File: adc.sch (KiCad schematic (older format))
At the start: 4 parts, among them U2 ADS114S08BIPBS

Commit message: added layout and online BOM viewer
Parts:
- C2, C3, C4: footprint (none) -> Capacitor_SMD:C_0805_2012Metric_Pad1.15x1.40mm_HandSolder
- U2: footprint PBS0032A_N -> footprints:ADS114S08BIPBS
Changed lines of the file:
@@
 $Descr A4 11693 8268
 encoding utf-8
-Sheet 2 3
+Sheet 3 3
 Title ""
 Date ""
@@
 AR Path="/5F3793F6/5F379707" Ref="U2"  Part="1"
 AR Path="/5F3BC575/5F379707" Ref="U3"  Part="1"
-F 0 "U2" H 4550 5488 60  0000 C CNN
+F 0 "U3" H 4550 5488 60  0000 C CNN
 F 1 "ADS114S08BIPBS" H 4550 5382 60  0000 C CNN
-F 2 "PBS0032A_N" H 4550 3640 60  0001 C CNN
+F 2 "footprints:ADS114S08BIPBS" H 4550 3640 60  0001 C CNN
 F 3 "" H 4550 3700 60  0000 C CNN
 	1    4550 3700
@@
 AR Path="/5F3793F6/5F37A378" Ref="C3"  Part="1"
 AR Path="/5F3BC575/5F37A378" Ref="C6"  Part="1"
-F 0 "C3" H 5992 2596 50  0000 L CNN
+F 0 "C6" H 5992 2596 50  0000 L CNN
 F 1 "1uF" H 5992 2505 50  0000 L CNN
-F 2 "" H 5900 2550 50  0001 C CNN
+F 2 "Capacitor_SMD:C_0805_2012Metric_Pad1.15x1.40mm_HandSolder" H 5900 2550 50  0001 C CNN
 F 3 "~" H 5900 2550 50  0001 C CNN
 	1    5900 2550
@@
 AR Path="/5F3793F6/5F37B0A0" Ref="C2"  Part="1"
 AR Path="/5F3BC575/5F37B0A0" Ref="C5"  Part="1"
-F 0 "C2" H 3242 4746 50  0000 L CNN
+F 0 "C5" H 3242 4746 50  0000 L CNN
 F 1 "330nF" H 3242 4655 50  0000 L CNN
-F 2 "" H 3150 4700 50  0001 C CNN
+F 2 "Capacitor_SMD:C_0805_2012Metric_Pad1.15x1.40mm_HandSolder" H 3150 4700 50  0001 C CNN
 F 3 "~" H 3150 4700 50  0001 C CNN
 	1    3150 4700
@@
 AR Path="/5F3793F6/5F389336" Ref="#PWR0105"  Part="1"
 AR Path="/5F3BC575/5F389336" Ref="#PWR0114"  Part="1"
-F 0 "#PWR0105" H 3150 4450 50  0001 C CNN
+F 0 "#PWR0114" H 3150 4450 50  0001 C CNN
 F 1 "+5V" H 3165 4773 50  0000 C CNN
 F 2 "" H 3150 4600 50  0001 C CNN
@@
 AR Path="/5F3793F6/5F38A513" Ref="#PWR0106"  Part="1"
 AR Path="/5F3BC575/5F38A513" Ref="#PWR0115"  Part="1"
-F 0 "#PWR0106" H 6000 4450 50  0001 C CNN
+F 0 "#PWR0115" H 6000 4450 50  0001 C CNN
 F 1 "+3.3V" H 6015 4773 50  0000 C CNN
 F 2 "" H 6000 4600 50  0001 C CNN
@@
 AR Path="/5F3793F6/5F38BAFC" Ref="C4"  Part="1"
 AR Path="/5F3BC575/5F38BAFC" Ref="C7"  Part="1"
-F 0 "C4" H 6092 4746 50  0000 L CNN
+F 0 "C7" H 6092 4746 50  0000 L CNN
 F 1 "0.1uF" H 6092 4655 50  0000 L CNN
-F 2 "" H 6000 4700 50  0001 C CNN
+F 2 "Capacitor_SMD:C_0805_2012Metric_Pad1.15x1.40mm_HandSolder" H 6000 4700 50  0001 C CNN
 F 3 "~" H 6000 4700 50  0001 C CNN
 	1    6000 4700
@@
 AR Path="/5F3793F6/5F38C9D2" Ref="#PWR0107"  Part="1"
 AR Path="/5F3BC575/5F38C9D2" Ref="#PWR0116"  Part="1"
-F 0 "#PWR0107" H 3150 4650 50  0001 C CNN
+F 0 "#PWR0116" H 3150 4650 50  0001 C CNN
 F 1 "GND" H 3155 4727 50  0000 C CNN
 F 2 "" H 3150 4900 50  0001 C CNN
@@
 AR Path="/5F3793F6/5F38E020" Ref="#PWR0108"  Part="1"
 AR Path="/5F3BC575/5F38E020" Ref="#PWR0117"  Part="1"
-F 0 "#PWR0108" H 6000 4850 50  0001 C CNN
+F 0 "#PWR0117" H 6000 4850 50  0001 C CNN
 F 1 "GND" H 6005 4927 50  0000 C CNN
 F 2 "" H 6000 5100 50  0001 C CNN
@@
 AR Path="/5F3793F6/5F38F179" Ref="#PWR0109"  Part="1"
 AR Path="/5F3BC575/5F38F179" Ref="#PWR0118"  Part="1"
-F 0 "#PWR0109" H 5900 2450 50  0001 C CNN
+F 0 "#PWR0118" H 5900 2450 50  0001 C CNN
 F 1 "GND" H 5905 2527 50  0000 C CNN
 F 2 "" H 5900 2700 50  0001 C CNN
@@
 AR Path="/5F3793F6/5F38F87E" Ref="#PWR0110"  Part="1"
 AR Path="/5F3BC575/5F38F87E" Ref="#PWR0119"  Part="1"
-F 0 "#PWR0110" H 5900 2950 50  0001 C CNN
+F 0 "#PWR0119" H 5900 2950 50  0001 C CNN
 F 1 "GND" H 5905 3027 50  0000 C CNN
 F 2 "" H 5900 3200 50  0001 C CNN
@@
 AR Path="/5F3793F6/5F39184B" Ref="#PWR0111"  Part="1"
 AR Path="/5F3BC575/5F39184B" Ref="#PWR0120"  Part="1"
-F 0 "#PWR0111" H 3100 2650 50  0001 C CNN
+F 0 "#PWR0120" H 3100 2650 50  0001 C CNN
 F 1 "GND" H 3105 2727 50  0000 C CNN
 F 2 "" H 3100 2900 50  0001 C CNN
@@
 AR Path="/5F3793F6/5F39364B" Ref="#PWR0112"  Part="1"
 AR Path="/5F3BC575/5F39364B" Ref="#PWR0121"  Part="1"
-F 0 "#PWR0112" H 6550 4350 50  0001 C CNN
+F 0 "#PWR0121" H 6550 4350 50  0001 C CNN
 F 1 "GND" H 6555 4427 50  0000 C CNN
 F 2 "" H 6550 4600 50  0001 C CNN
@@
 AR Path="/5F3793F6/5F394587" Ref="#PWR0113"  Part="1"
 AR Path="/5F3BC575/5F394587" Ref="#PWR0122"  Part="1"
-F 0 "#PWR0113" H 6450 2550 50  0001 C CNN
+F 0 "#PWR0122" H 6450 2550 50  0001 C CNN
 F 1 "+3.3V" H 6465 2873 50  0000 C CNN
 F 2 "" H 6450 2700 50  0001 C CNN

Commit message: ads1261
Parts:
- removed C2: 330nF, Capacitor_SMD:C_0805_2012Metric_Pad1.15x1.40mm_HandSolder, symbol Device:C_Small
- removed C3: 1uF, Capacitor_SMD:C_0805_2012Metric_Pad1.15x1.40mm_HandSolder, symbol Device:C_Small
- removed C4: 0.1uF, Capacitor_SMD:C_0805_2012Metric_Pad1.15x1.40mm_HandSolder, symbol Device:C_Small
- removed U2: ADS114S08BIPBS, footprints:ADS114S08BIPBS, symbol ads114s08b:ADS114S08BIPBS
- added C202, C204, C205: 1uF, Capacitor_SMD:C_0603_1608Metric, symbol Device:C
- added C301: 4.7nF C0G, Capacitor_SMD:C_0603_1608Metric, symbol Device:C
- added C303, C306: 10uF, Capacitor_SMD:C_0603_1608Metric, symbol Device:C
- added U301: ADS1261BIRHBR, footprints:ADS1261BIRHBR, symbol ads1261:ADS1261BIRHBR
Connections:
- net labels added: AIN-, AIN0, AIN1, AIN2, AIN3, AIN4, AIN5, AIN6, AIN7, AIN8, AIN9, BYPASS, CAP+, CAP-, GNDREF, REF2.5V
- net labels removed: +2.5V_OUT, 0, 1, 10, 11, 2, 3, 4, 5, 6, 7, 8, 9, A0, A1, A10, A11, A2, A3, A4, A5, A6, A7, A8, A9
- wire segments 31 -> 30
- no-connect marks 4 -> 1
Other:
- note removed: "Calculating your voltage ranges:\nhttps://www.ti.com/tool/ADS124S08-EXCEL-CALC-TOOL"
- note removed: "The ADC is configured to operate in SPI command only mode\n"
- note removed: "This 2.5V out provides a good negative input\nfor sensors that rely on the PGA"
- note removed: "We will select the internal\n2.5V reference"
- note removed: "You call it "parasitic capacitance"\nTI calls it "integrated EMI filter"\n\nEither way I decided not to put RC filters on the ADC inputs since Freq. \nResponse is capped at 40 MHz\n (radio is 400ish Mhz). \nIf there is noise we can add external low \npass filters\n or use differential inputs to filter out common mode noise"

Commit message: boi did i cut up that ground plane
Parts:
- added R201: 4.7K, Resistor_SMD:R_0805_2012Metric_Pad1.15x1.40mm_HandSolder, symbol Device:R_US
- C202, C204, C205, C301, C303, C306: footprint Capacitor_SMD:C_0603_1608Metric -> Capacitor_SMD:C_0805_2012Metric_Pad1.15x1.40mm_HandSolder
- U301: footprint footprints:ADS1261BIRHBR -> Package_DFN_QFN:Texas_S-PVQFN-N32_EP3.45x3.45mm
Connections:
- net +3V3: now also R201.1
- net ~CS: now also R201.2
- net AIN- renamed AINCOM
- no-connect marks 1 -> 5

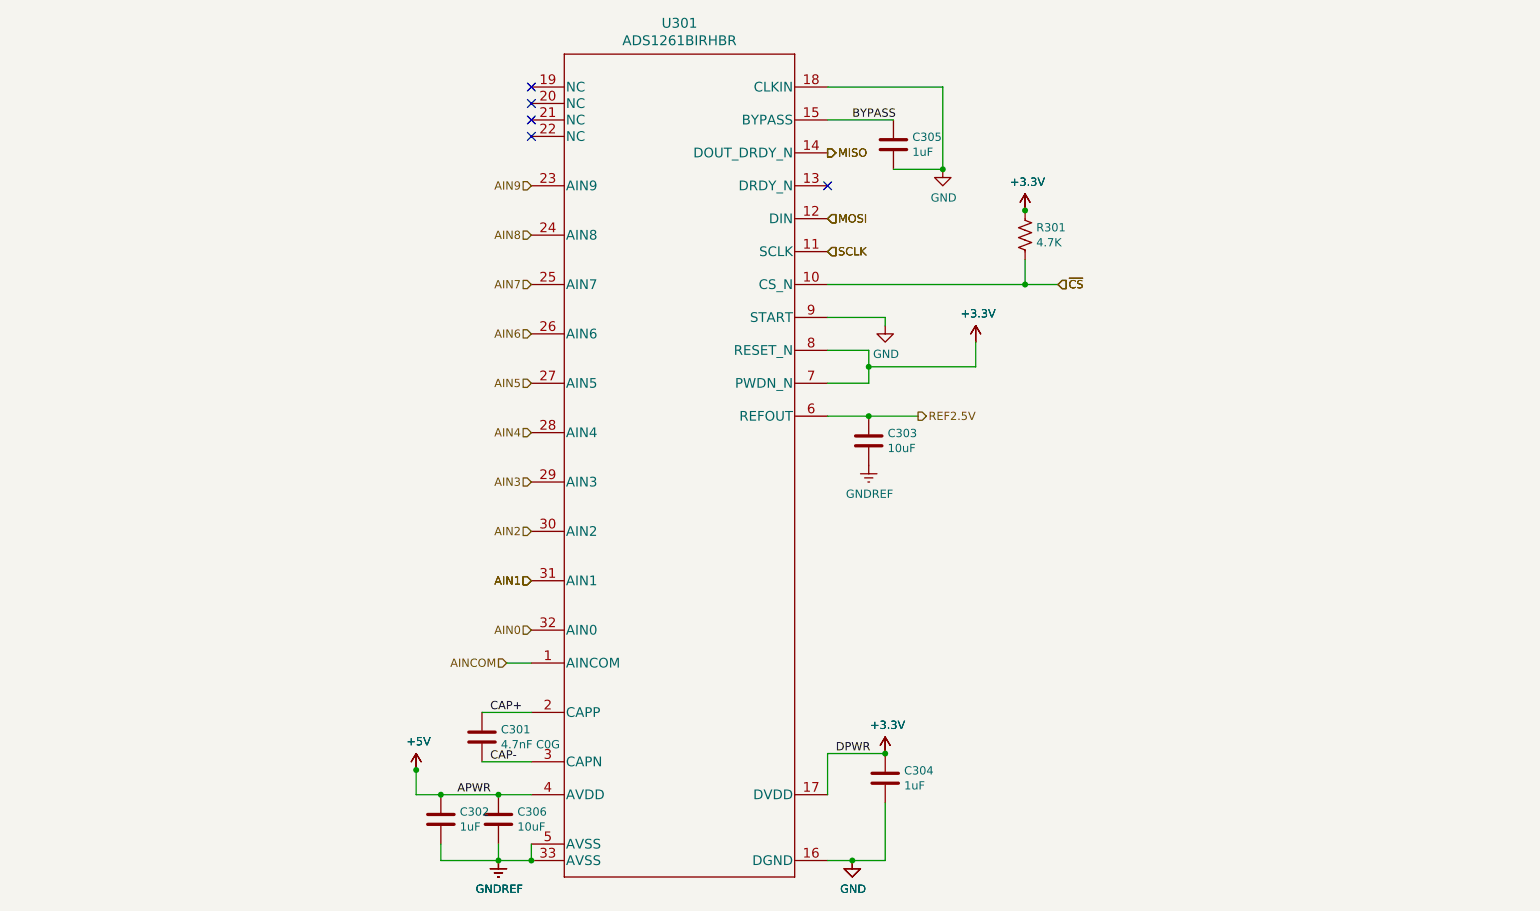
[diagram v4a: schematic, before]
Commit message: add silkscreen labels
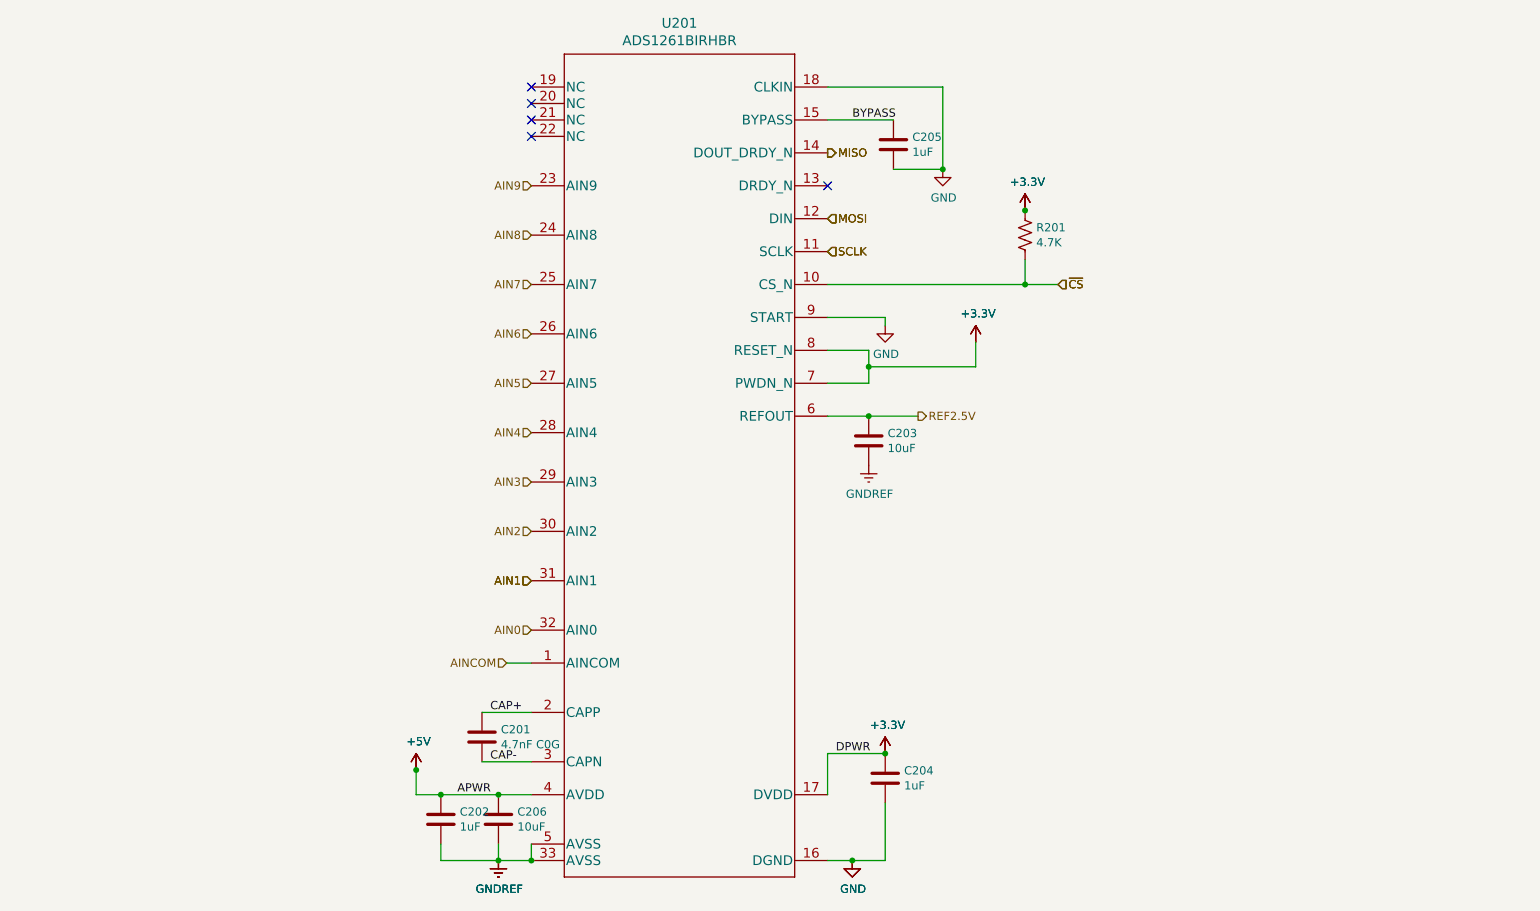
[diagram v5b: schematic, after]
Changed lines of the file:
@@
 $Descr A4 11693 8268
 encoding utf-8
-Sheet 3 4
+Sheet 2 4
 Title ""
 Date ""
@@
 AR Path="/5F4A8EC5/5F4D602B" Ref="#PWR0107"  Part="1"
 AR Path="/5F4D3EB7/5F4D602B" Ref="#PWR0123"  Part="1"
-F 0 "#PWR0123" H 3200 5600 50  0001 C CNN
+F 0 "#PWR0107" H 3200 5600 50  0001 C CNN
 F 1 "+5V" H 3215 5923 50  0000 C CNN
 F 2 "" H 3200 5750 50  0001 C CNN
@@
 AR Path="/5F4A8EC5/5F4ADFB1" Ref="#PWR0108"  Part="1"
 AR Path="/5F4D3EB7/5F4ADFB1" Ref="#PWR0124"  Part="1"
-F 0 "#PWR0124" H 3700 6050 50  0001 C CNN
+F 0 "#PWR0108" H 3700 6050 50  0001 C CNN
 F 1 "GNDREF" H 3705 6127 50  0000 C CNN
 F 2 "" H 3700 6300 50  0001 C CNN
@@
 AR Path="/5F4A8EC5/5F4AF0E5" Ref="#PWR0109"  Part="1"
 AR Path="/5F4D3EB7/5F4AF0E5" Ref="#PWR0125"  Part="1"
-F 0 "#PWR0125" H 5850 6050 50  0001 C CNN
+F 0 "#PWR0109" H 5850 6050 50  0001 C CNN
 F 1 "GND" H 5855 6127 50  0000 C CNN
 F 2 "" H 5850 6300 50  0001 C CNN
@@
 AR Path="/5F4A8EC5/5F4B0081" Ref="#PWR0110"  Part="1"
 AR Path="/5F4D3EB7/5F4B0081" Ref="#PWR0126"  Part="1"
-F 0 "#PWR0126" H 6050 5500 50  0001 C CNN
+F 0 "#PWR0110" H 6050 5500 50  0001 C CNN
 F 1 "+3.3V" H 6065 5823 50  0000 C CNN
 F 2 "" H 6050 5650 50  0001 C CNN
@@
 AR Path="/5F4A8EC5/5F4D6031" Ref="#PWR0113"  Part="1"
 AR Path="/5F4D3EB7/5F4D6031" Ref="#PWR0129"  Part="1"
-F 0 "#PWR0129" H 6600 3000 50  0001 C CNN
+F 0 "#PWR0113" H 6600 3000 50  0001 C CNN
 F 1 "+3.3V" H 6615 3323 50  0000 C CNN
 F 2 "" H 6600 3150 50  0001 C CNN
@@
 AR Path="/5F4A8EC5/5F4B6004" Ref="C205"  Part="1"
 AR Path="/5F4D3EB7/5F4B6004" Ref="C305"  Part="1"
-F 0 "C305" H 6215 1996 50  0000 L CNN
+F 0 "C205" H 6215 1996 50  0000 L CNN
 F 1 "1uF" H 6215 1905 50  0000 L CNN
 F 2 "Capacitor_SMD:C_0805_2012Metric_Pad1.15x1.40mm_HandSolder" H 6138 1800 50  0001 C CNN
@@
 AR Path="/5F4D3EB7/5F4A90E1" Ref="U301"  Part="1"
 AR Path="/5F4A8EC5/5F4A90E1" Ref="U201"  Part="1"
-F 0 "U301" H 4800 6588 60  0000 C CNN
+F 0 "U201" H 4800 6588 60  0000 C CNN
 F 1 "ADS1261BIRHBR" H 4800 6482 60  0000 C CNN
 F 2 "Package_DFN_QFN:Texas_S-PVQFN-N32_EP3.45x3.45mm" H 4800 3840 60  0001 C CNN
@@
 AR Path="/5F4D3EB7/5F4AAB9D" Ref="C301"  Part="1"
 AR Path="/5F4A8EC5/5F4AAB9D" Ref="C201"  Part="1"
-F 0 "C301" H 3715 5596 50  0000 L CNN
+F 0 "C201" H 3715 5596 50  0000 L CNN
 F 1 "4.7nF C0G" H 3715 5505 50  0000 L CNN
 F 2 "Capacitor_SMD:C_0805_2012Metric_Pad1.15x1.40mm_HandSolder" H 3638 5400 50  0001 C CNN
@@
 AR Path="/5F4D3EB7/5F4ABE0F" Ref="#PWR0131"  Part="1"
 AR Path="/5F4A8EC5/5F4ABE0F" Ref="#PWR0115"  Part="1"
-F 0 "#PWR0131" H 3200 5600 50  0001 C CNN
+F 0 "#PWR0115" H 3200 5600 50  0001 C CNN
 F 1 "+5V" H 3215 5923 50  0000 C CNN
 F 2 "" H 3200 5750 50  0001 C CNN
@@
 AR Path="/5F4D3EB7/5F4D602C" Ref="#PWR0132"  Part="1"
 AR Path="/5F4A8EC5/5F4D602C" Ref="#PWR0116"  Part="1"
-F 0 "#PWR0132" H 3700 6050 50  0001 C CNN
+F 0 "#PWR0116" H 3700 6050 50  0001 C CNN
 F 1 "GNDREF" H 3705 6127 50  0000 C CNN
 F 2 "" H 3700 6300 50  0001 C CNN
@@
 AR Path="/5F4D3EB7/5F4D602D" Ref="#PWR0133"  Part="1"
 AR Path="/5F4A8EC5/5F4D602D" Ref="#PWR0117"  Part="1"
-F 0 "#PWR0133" H 5850 6050 50  0001 C CNN
+F 0 "#PWR0117" H 5850 6050 50  0001 C CNN
 F 1 "GND" H 5855 6127 50  0000 C CNN
 F 2 "" H 5850 6300 50  0001 C CNN
@@
 AR Path="/5F4D3EB7/5F4D602E" Ref="#PWR0134"  Part="1"
 AR Path="/5F4A8EC5/5F4D602E" Ref="#PWR0118"  Part="1"
-F 0 "#PWR0134" H 6050 5500 50  0001 C CNN
+F 0 "#PWR0118" H 6050 5500 50  0001 C CNN
 F 1 "+3.3V" H 6065 5823 50  0000 C CNN
 F 2 "" H 6050 5650 50  0001 C CNN
@@
 AR Path="/5F4D3EB7/5F4D6030" Ref="#PWR0136"  Part="1"
 AR Path="/5F4A8EC5/5F4D6030" Ref="#PWR0120"  Part="1"
-F 0 "#PWR0136" H 6050 2800 50  0001 C CNN
+F 0 "#PWR0120" H 6050 2800 50  0001 C CNN
 F 1 "GND" H 6055 2877 50  0000 C CNN
 F 2 "" H 6050 3050 50  0001 C CNN
@@
 AR Path="/5F4D3EB7/5F4B3879" Ref="#PWR0137"  Part="1"
 AR Path="/5F4A8EC5/5F4B3879" Ref="#PWR0121"  Part="1"
-F 0 "#PWR0137" H 6600 3000 50  0001 C CNN
+F 0 "#PWR0121" H 6600 3000 50  0001 C CNN
 F 1 "+3.3V" H 6615 3323 50  0000 C CNN
 F 2 "" H 6600 3150 50  0001 C CNN
@@
 AR Path="/5F4A8EC5/5F4B7BDA" Ref="C202"  Part="1"
 AR Path="/5F4D3EB7/5F4B7BDA" Ref="C302"  Part="1"
-F 0 "C302" H 3465 6096 50  0000 L CNN
+F 0 "C202" H 3465 6096 50  0000 L CNN
 F 1 "1uF" H 3465 6005 50  0000 L CNN
 F 2 "Capacitor_SMD:C_0805_2012Metric_Pad1.15x1.40mm_HandSolder" H 3388 5900 50  0001 C CNN
@@
 AR Path="/5F4A8EC5/5F4CD7CF" Ref="C204"  Part="1"
 AR Path="/5F4D3EB7/5F4CD7CF" Ref="C304"  Part="1"
-F 0 "C304" H 6165 5846 50  0000 L CNN
+F 0 "C204" H 6165 5846 50  0000 L CNN
 F 1 "1uF" H 6165 5755 50  0000 L CNN
 F 2 "Capacitor_SMD:C_0805_2012Metric_Pad1.15x1.40mm_HandSolder" H 6088 5650 50  0001 C CNN
@@
 AR Path="/5F4D3EB7/5F4D602F" Ref="#PWR0135"  Part="1"
 AR Path="/5F4A8EC5/5F4D602F" Ref="#PWR0119"  Part="1"
-F 0 "#PWR0135" H 6400 1850 50  0001 C CNN
+F 0 "#PWR0119" H 6400 1850 50  0001 C CNN
 F 1 "GND" H 6405 1927 50  0000 C CNN
 F 2 "" H 6400 2100 50  0001 C CNN
@@
 AR Path="/5F4A8EC5/5F4C03A0" Ref="#PWR0111"  Part="1"
 AR Path="/5F4D3EB7/5F4C03A0" Ref="#PWR0112"  Part="1"
-F 0 "#PWR0112" H 5950 3650 50  0001 C CNN
+F 0 "#PWR0111" H 5950 3650 50  0001 C CNN
 F 1 "GNDREF" H 5955 3727 50  0000 C CNN
 F 2 "" H 5950 3900 50  0001 C CNN
@@
 AR Path="/5F4D3EB7/5F4C2005" Ref="C306"  Part="1"
 AR Path="/5F4A8EC5/5F4C2005" Ref="C206"  Part="1"
-F 0 "C306" H 3815 6096 50  0000 L CNN
+F 0 "C206" H 3815 6096 50  0000 L CNN
 F 1 "10uF" H 3815 6005 50  0000 L CNN
 F 2 "Capacitor_SMD:C_0805_2012Metric_Pad1.15x1.40mm_HandSolder" H 3738 5900 50  0001 C CNN
@@
 AR Path="/5F4D3EB7/5F4B8109" Ref="C303"  Part="1"
 AR Path="/5F4A8EC5/5F4B8109" Ref="C203"  Part="1"
-F 0 "C303" H 6065 3796 50  0000 L CNN
+F 0 "C203" H 6065 3796 50  0000 L CNN
 F 1 "10uF" H 6065 3705 50  0000 L CNN
 F 2 "Capacitor_SMD:C_0805_2012Metric_Pad1.15x1.40mm_HandSolder" H 5988 3600 50  0001 C CNN
@@
 AR Path="/5F4A8EC5/5F6B4ED7" Ref="R201"  Part="1"
 AR Path="/5F4D3EB7/5F6B4ED7" Ref="R301"  Part="1"
-F 0 "R301" H 6968 2546 50  0000 L CNN
+F 0 "R201" H 6968 2546 50  0000 L CNN
 F 1 "4.7K" H 6968 2455 50  0000 L CNN
 F 2 "Resistor_SMD:R_0805_2012Metric_Pad1.15x1.40mm_HandSolder" V 6940 2490 50  0001 C CNN
@@
 AR Path="/5F4A8EC5/5F6B97FB" Ref="#PWR0104"  Part="1"
 AR Path="/5F4D3EB7/5F6B97FB" Ref="#PWR0128"  Part="1"
-F 0 "#PWR0128" H 6900 2200 50  0001 C CNN
+F 0 "#PWR0104" H 6900 2200 50  0001 C CNN
 F 1 "+3.3V" H 6915 2523 50  0000 C CNN
 F 2 "" H 6900 2350 50  0001 C CNN
@@
 AR Path="/5F4D3EB7/5F6B9801" Ref="#PWR0130"  Part="1"
 AR Path="/5F4A8EC5/5F6B9801" Ref="#PWR0105"  Part="1"
-F 0 "#PWR0130" H 6900 2200 50  0001 C CNN
+F 0 "#PWR0105" H 6900 2200 50  0001 C CNN
 F 1 "+3.3V" H 6915 2523 50  0000 C CNN
 F 2 "" H 6900 2350 50  0001 C CNN
